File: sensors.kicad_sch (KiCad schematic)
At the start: 46 parts

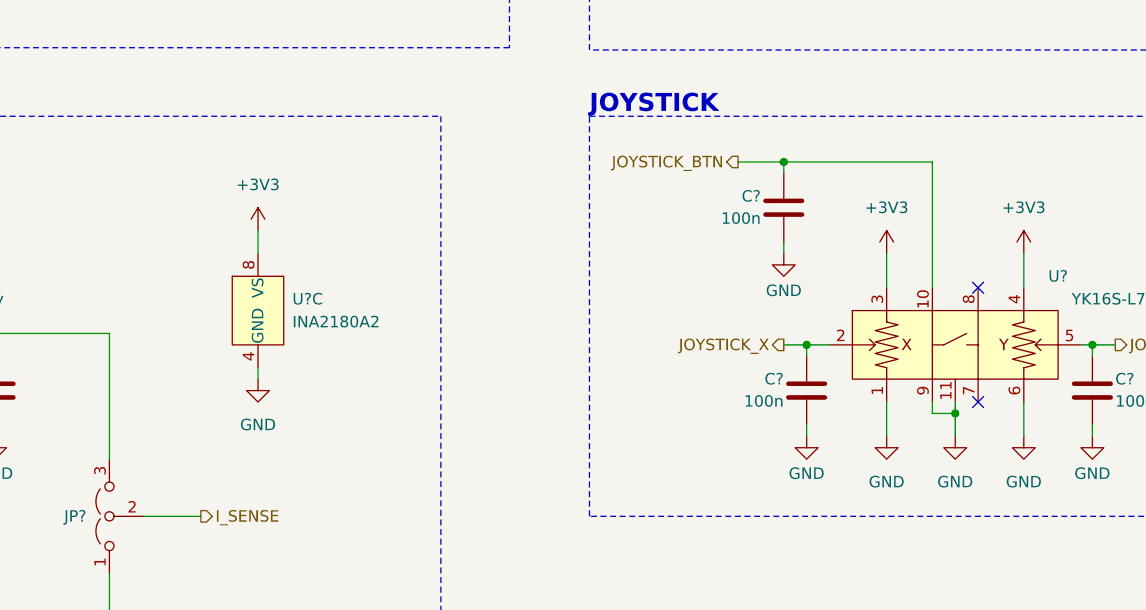
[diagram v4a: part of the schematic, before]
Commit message: Fixed some schematic issues
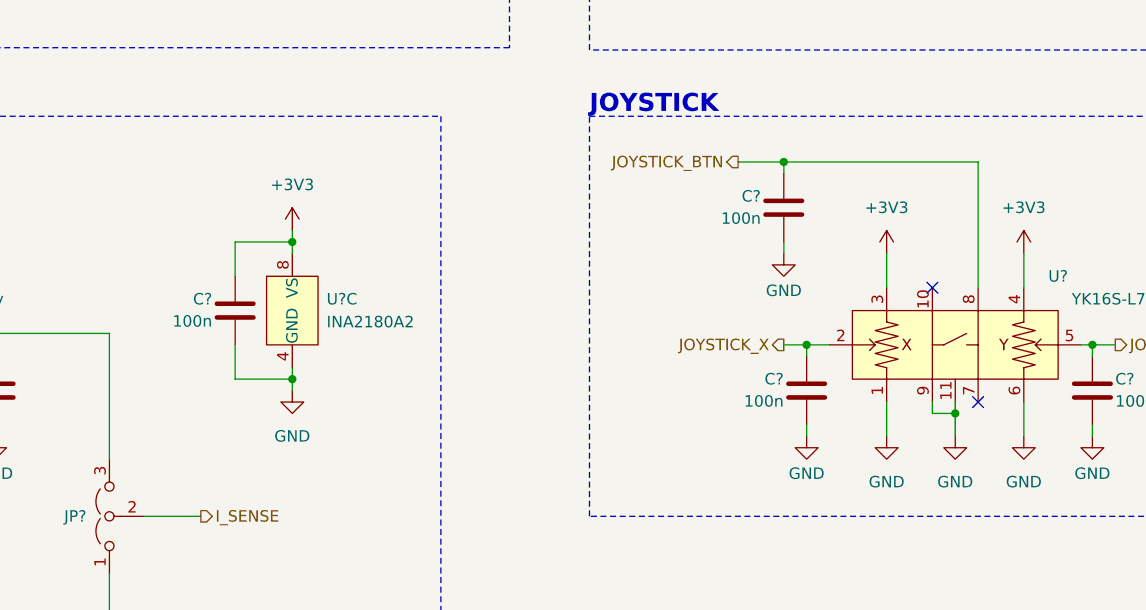
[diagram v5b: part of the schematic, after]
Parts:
- added C?: 100n, Capacitor_SMD:C_0402_1005Metric, symbol Device:C
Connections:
- net +3V3: now also C?.1
- net GND: now also C?.2
- net JOYSTICK_BTN: now also U?.8; no longer U?.10
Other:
- moved on the sheet: U?C
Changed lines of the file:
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@@
 	)
 	(junction
+		(at 153.67 113.03)
+		(diameter 0)
+		(color 0 0 0 0)
+	)
+	(junction
 		(at 72.39 166.37)
 		(diameter 0)
@@
 	)
 	(junction
+		(at 153.67 128.27)
+		(diameter 0)
+		(color 0 0 0 0)
+	)
+	(junction
 		(at 66.04 148.59)
 		(diameter 0)
@@
 	)
 	(no_connect
-		(at 80.01 54.61)
+		(at 224.79 118.11)
 	)
 	(no_connect
-		(at 229.87 118.11)
+		(at 80.01 54.61)
 	)
 	(wire
 		(pts
-			(xy 149.86 111.76) (xy 149.86 114.3)
+			(xy 153.67 111.76) (xy 153.67 113.03)
 		)
 		(stroke
@@
 		)
 	)
-	(wire
+	(polyline
 		(pts
-			(xy 224.79 104.14) (xy 224.79 118.11)
+			(xy 40.64 66.04) (xy 38.1 80.01)
 		)
 		(stroke
 			(width 0)
-			(type default)
+			(type dash)
 		)
 	)
-	(polyline
+	(wire
 		(pts
-			(xy 40.64 66.04) (xy 38.1 80.01)
+			(xy 49.53 118.11) (xy 49.53 125.73)
 		)
 		(stroke
 			(width 0)
-			(type dash)
+			(type default)
 		)
 	)
 	(wire
 		(pts
-			(xy 49.53 118.11) (xy 49.53 125.73)
+			(xy 153.67 113.03) (xy 153.67 114.3)
 		)
 		(stroke
@@
 	(wire
 		(pts
-			(xy 149.86 127) (xy 149.86 128.27)
+			(xy 153.67 127) (xy 153.67 128.27)
 		)
 		(stroke
@@
 	(wire
 		(pts
+			(xy 147.32 124.46) (xy 147.32 128.27)
+		)
+		(stroke
+			(width 0)
+			(type default)
+		)
+	)
+	(wire
+		(pts
+			(xy 153.67 129.54) (xy 153.67 128.27)
+		)
+		(stroke
+			(width 0)
+			(type default)
+		)
+	)
+	(wire
+		(pts
 			(xy 73.66 31.75) (xy 73.66 30.48)
 		)
@@
 	(wire
 		(pts
+			(xy 147.32 116.84) (xy 147.32 113.03)
+		)
+		(stroke
+			(width 0)
+			(type default)
+		)
+	)
+	(wire
+		(pts
 			(xy 134.62 29.21) (xy 134.62 30.48)
 		)
@@
 	(wire
 		(pts
+			(xy 229.87 104.14) (xy 229.87 118.11)
+		)
+		(stroke
+			(width 0)
+			(type default)
+		)
+	)
+	(wire
+		(pts
+			(xy 147.32 113.03) (xy 153.67 113.03)
+		)
+		(stroke
+			(width 0)
+			(type default)
+		)
+	)
+	(wire
+		(pts
 			(xy 64.77 30.48) (xy 58.42 30.48)
 		)
@@
 	(wire
 		(pts
-			(xy 208.28 104.14) (xy 224.79 104.14)
+			(xy 208.28 104.14) (xy 229.87 104.14)
 		)
 		(stroke
@@
 	(wire
 		(pts
+			(xy 147.32 128.27) (xy 153.67 128.27)
+		)
+		(stroke
+			(width 0)
+			(type default)
+		)
+	)
+	(wire
+		(pts
 			(xy 66.04 148.59) (xy 72.39 148.59)
 		)
@@
 	(symbol
 		(lib_id "ProjectAmplifiers:INA2180A2_VSSOP-8")
-		(at 149.86 120.65 0)
+		(at 153.67 120.65 0)
 		(unit 3)
 		(exclude_from_sim no)
@@
 		(fields_autoplaced yes)
 		(property "Reference" "U?"
-			(at 153.67 119.3799 0)
+			(at 157.48 119.3799 0)
 			(effects
 				(font
@@
 		)
 		(property "Value" "INA2180A2"
-			(at 153.67 121.9199 0)
+			(at 157.48 121.9199 0)
 			(effects
 				(font
@@
 		)
 		(property "Footprint" "Package_SO:VSSOP-8_3x3mm_P0.65mm"
-			(at 150.495 120.65 0)
+			(at 154.305 120.65 0)
 			(effects
 				(font
@@
 		)
 		(property "Datasheet" "http://www.ti.com/lit/ds/symlink/ina180.pdf"
-			(at 154.305 120.3325 0)
+			(at 158.115 120.3325 0)
 			(effects
 				(font
@@
 		)
 		(property "Description" "Current Sense Amplifier, 1 Circuit, Rail-to-Rail, 26V, Gain 50 V/V, SOT-23-5"
-			(at 149.86 120.3325 0)
+			(at 153.67 120.3325 0)
 			(effects
 				(font
@@
 		)
 		(property "Sim.Library" "ina180a2.lib"
-			(at 149.86 120.65 0)
+			(at 153.67 120.65 0)
 			(effects
 				(font
@@
 		)
 		(property "Sim.Name" "INA2180A2"
-			(at 149.86 120.65 0)
+			(at 153.67 120.65 0)
 			(effects
 				(font
@@
 		)
 		(property "Sim.Device" "SUBCKT"
-			(at 149.86 120.65 0)
+			(at 153.67 120.65 0)
 			(effects
 				(font
@@
 		)
 		(property "Sim.Pins" "1=OUT1 2=IN1- 3=IN1+ 4=GND 5=IN2+ 6=IN2- 7=OUT2 8=VCC"
-			(at 149.86 120.3325 0)
+			(at 153.67 120.3325 0)
 			(effects
 				(font
@@
 	(symbol
 		(lib_id "power:GND")
-		(at 149.86 128.27 0)
+		(at 153.67 129.54 0)
 		(unit 1)
 		(exclude_from_sim no)
@@
 		(fields_autoplaced yes)
 		(property "Reference" "#PWR?"
-			(at 149.86 134.62 0)
+			(at 153.67 135.89 0)
 			(effects
 				(font
@@
 		)
 		(property "Value" "GND"
-			(at 149.86 133.35 0)
+			(at 153.67 134.62 0)
 			(effects
 				(font
@@
 		)
 		(property "Footprint" ""
-			(at 149.86 128.27 0)
+			(at 153.67 129.54 0)
 			(effects
 				(font
@@
 		)
 		(property "Datasheet" ""
-			(at 149.86 128.27 0)
+			(at 153.67 129.54 0)
 			(effects
 				(font
@@
 		)
 		(property "Description" "Power symbol creates a global label with name \"GND\" , ground"
-			(at 149.86 128.27 0)
+			(at 153.67 129.54 0)
 			(effects
 				(font
@@
 	(symbol
 		(lib_id "power:+3V3")
-		(at 149.86 111.76 0)
+		(at 153.67 111.76 0)
 		(unit 1)
 		(exclude_from_sim no)
@@
 		(fields_autoplaced yes)
 		(property "Reference" "#PWR?"
-			(at 149.86 115.57 0)
+			(at 153.67 115.57 0)
 			(effects
 				(font
@@
 		)
 		(property "Value" "+3V3"
-			(at 149.86 106.68 0)
+			(at 153.67 106.68 0)
 			(effects
 				(font
@@
 		)
 		(property "Footprint" ""
-			(at 149.86 111.76 0)
+			(at 153.67 111.76 0)
 			(effects
 				(font
@@
 		)
 		(property "Datasheet" ""
-			(at 149.86 111.76 0)
+			(at 153.67 111.76 0)
 			(effects
 				(font
@@
 		)
 		(property "Description" "Power symbol creates a global label with name \"+3V3\""
-			(at 149.86 111.76 0)
+			(at 153.67 111.76 0)
 			(effects
 				(font
@@
 			(project "Educational-Board_MainBoard"
 				(path "/835b4df9-7d62-45f4-81d2-5a64fbc86f3c/fff2b078-1c83-42d8-b24c-4d93ca90abbb"
+					(reference "C?")
+					(unit 1)
+				)
+			)
+		)
+	)
+	(symbol
+		(lib_id "Device:C")
+		(at 147.32 120.65 0)
+		(mirror y)
+		(unit 1)
+		(exclude_from_sim no)
+		(in_bom yes)
+		(on_board yes)
+		(dnp no)
+		(property "Reference" "C?"
+			(at 144.78 119.38 0)
+			(effects
+				(font
+					(size 1.27 1.27)
+				)
+				(justify left)
+			)
+		)
+		(property "Value" "100n"
+			(at 144.78 121.8454 0)
+			(effects
+				(font
+					(size 1.27 1.27)
+				)
+				(justify left)
+			)
+		)
+		(property "Footprint" "Capacitor_SMD:C_0402_1005Metric"
+			(at 146.3548 124.46 0)
+			(effects
+				(font
+					(size 1.27 1.27)
+				)
+				(hide yes)
+			)
+		)
+		(property "Datasheet" "~"
+			(at 147.32 120.65 0)
+			(effects
+				(font
+					(size 1.27 1.27)
+				)
+				(hide yes)
+			)
+		)
+		(property "Description" "Unpolarized capacitor"
+			(at 147.32 120.65 0)
+			(effects
+				(font
+					(size 1.27 1.27)
+				)
+				(hide yes)
+			)
+		)
+		(property "LCSC" "C1525"
+			(at 147.32 120.65 0)
+			(effects
+				(font
+					(size 1.27 1.27)
+				)
+				(hide yes)
+			)
+		)
+		(pin "1"
+		)
+		(pin "2"
+		)
+		(instances
+			(project "Educational-Board_MainBoard"
+				(path "/835b4df9-7d62-45f4-81d2-5a64fbc86f3c/fff2b078-1c83-42d8-b24c-4d93ca90abbb"

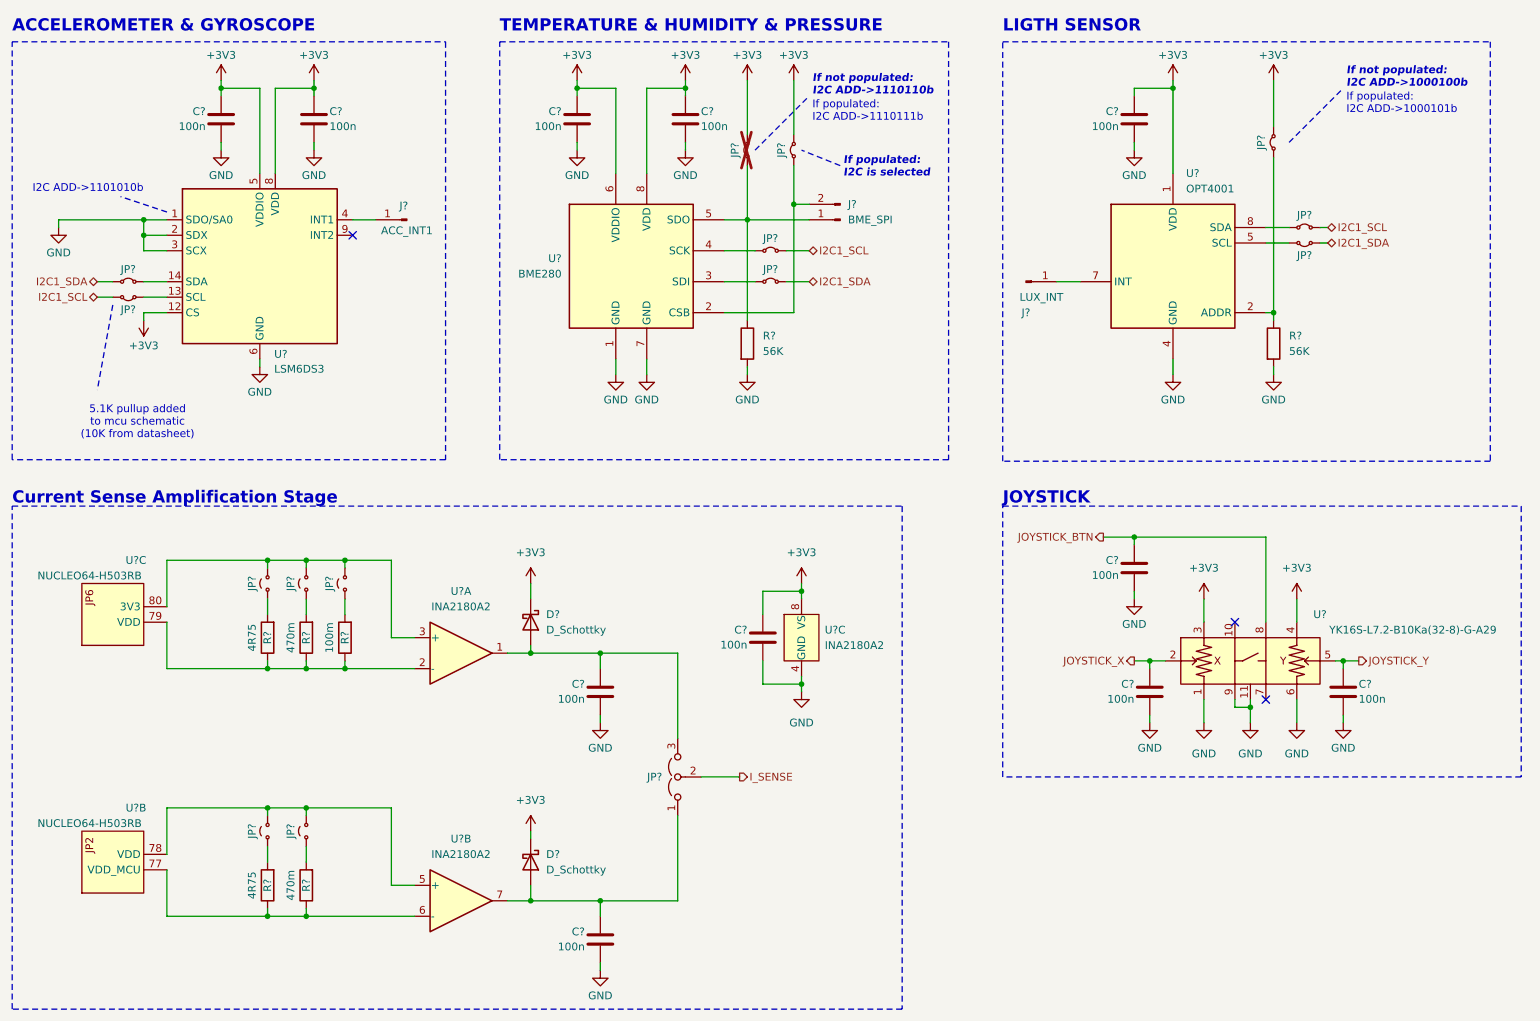
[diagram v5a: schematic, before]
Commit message: Referenced the shematic and started the sourcing part
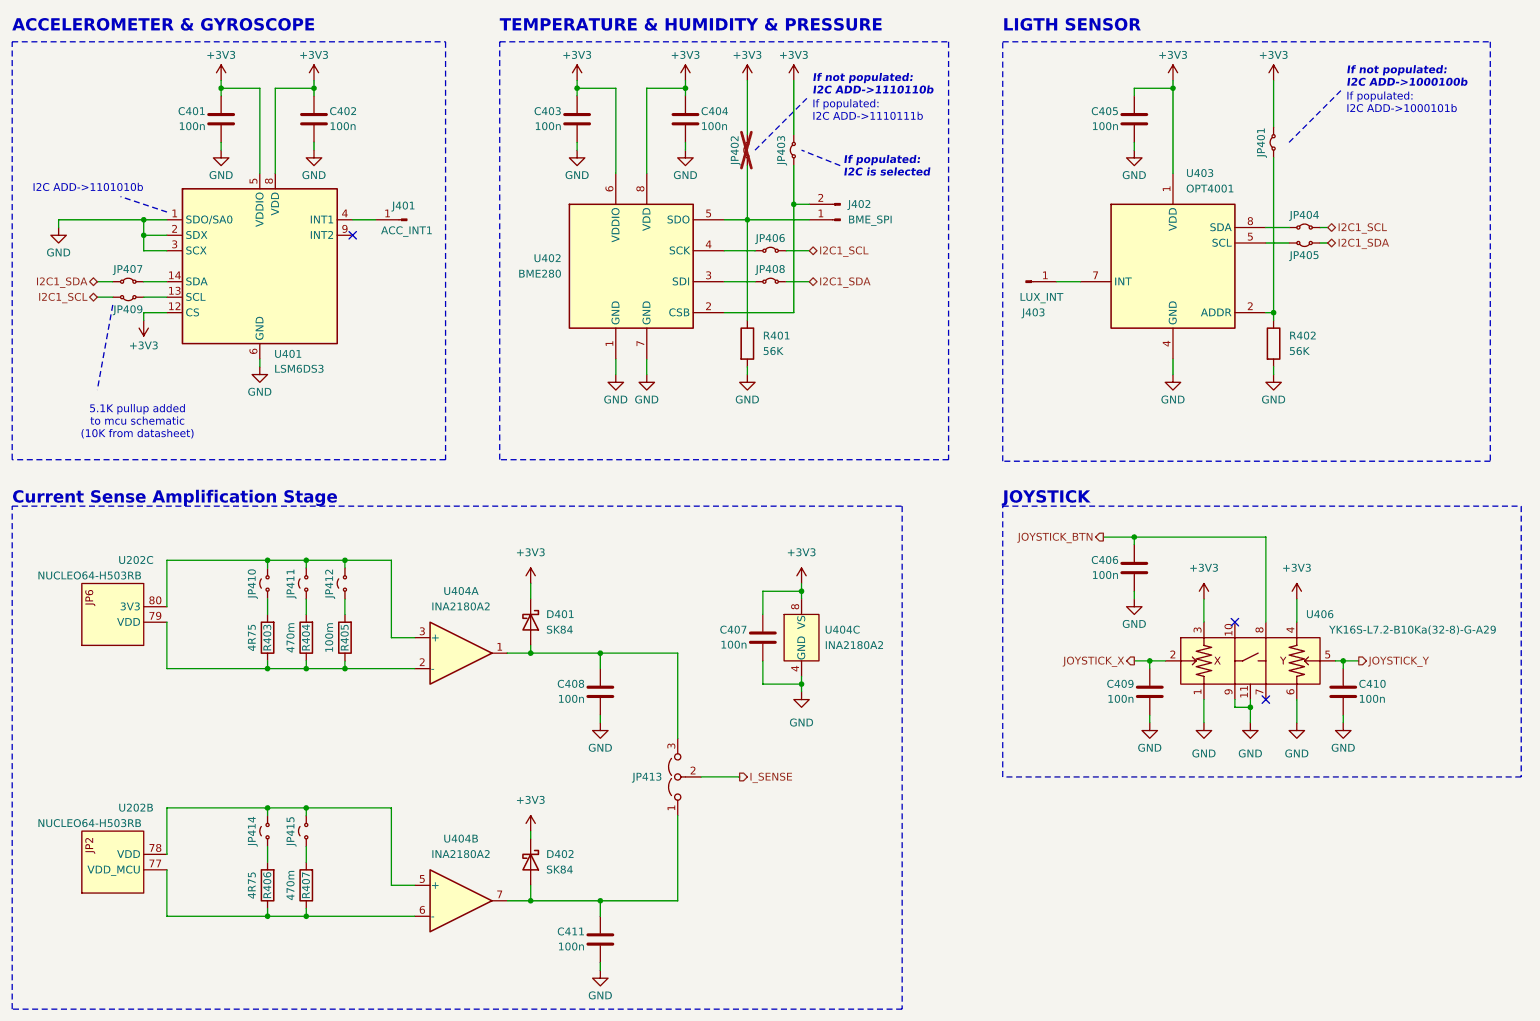
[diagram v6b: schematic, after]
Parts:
- C401, C402, C403, C404, C405, C406, C407, C408, C409, C410, C411: renamed from C?; footprint Capacitor_SMD:C_0402_1005Metric -> Capacitor_SMD:C_0603_1608Metric_Pad1.08x0.95mm_HandSolder; LCSC C1525 -> C14663
- D401, D402: renamed from D?; value D_Schottky -> SK84; footprint (none) -> Diode_SMD:D_SMB_Handsoldering; LCSC (none) -> C2922187
- J401, J403: renamed from J?; footprint (none) -> Connector_PinHeader_2.54mm:PinHeader_1x01_P2.54mm_Vertical; LCSC (none) -> C492400
- J402: renamed from J?; footprint (none) -> Connector_PinHeader_2.54mm:PinHeader_1x02_P2.54mm_Vertical; LCSC (none) -> C492401
- JP410, JP411, JP412, JP414, JP415: renamed from JP?; LCSC (none) -> C492401
- JP413: renamed from JP?; LCSC (none) -> C492402
- R401, R402: renamed from R?; footprint (none) -> Resistor_SMD:R_0603_1608Metric_Pad0.98x0.95mm_HandSolder; LCSC (none) -> C23206
- R403, R404, R405, R406, R407: renamed from R?; footprint (none) -> Resistor_SMD:R_0603_1608Metric_Pad0.98x0.95mm_HandSolder
- U202: renamed from U?; now left out of the parts list
- U402: renamed from U?; LCSC (none) -> C92489
- U403: renamed from U?; LCSC (none) -> C17612395
- U404: renamed from U?; LCSC (none) -> C2058508
- gave numbers to parts that had none: 11

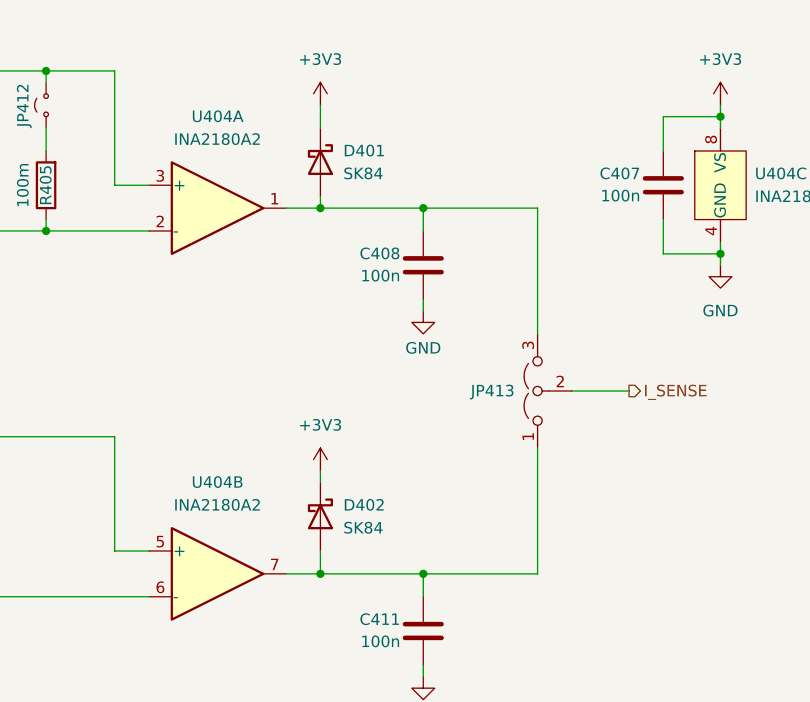
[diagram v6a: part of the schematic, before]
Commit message: added some lcsc codes, changed reverse voltage protection with a diode
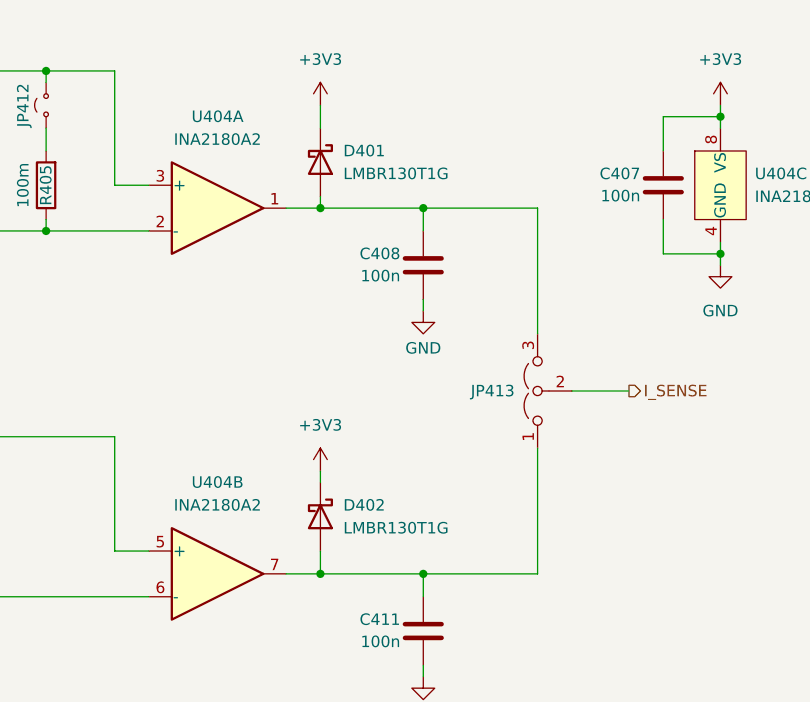
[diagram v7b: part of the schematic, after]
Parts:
- D401, D402: value SK84 -> LMBR130T1G; footprint Diode_SMD:D_SMB_Handsoldering -> Diode_SMD:D_SOD-123; LCSC C2922187 -> C48974
- JP401, JP402, JP403, JP404, JP405, JP406, JP407, JP408, JP409: footprint (none) -> Resistor_SMD:R_0603_1608Metric_Pad0.98x0.95mm_HandSolder; LCSC (none) -> C21189
